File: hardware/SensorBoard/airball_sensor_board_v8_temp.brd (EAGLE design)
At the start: 19.1 x 6.3 mm, 3 parts, among them J2 Vertical Qwiic Connector, U1 TMP102

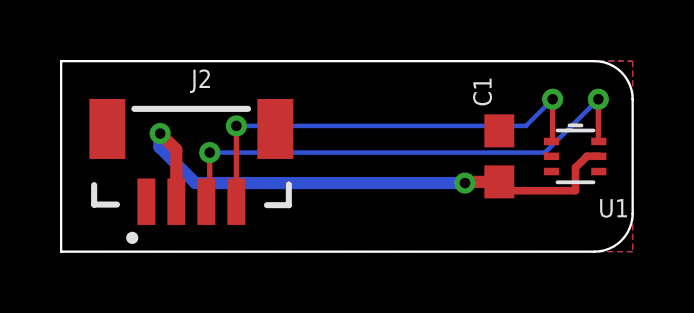
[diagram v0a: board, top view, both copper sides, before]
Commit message: Completed temperature sensor board.
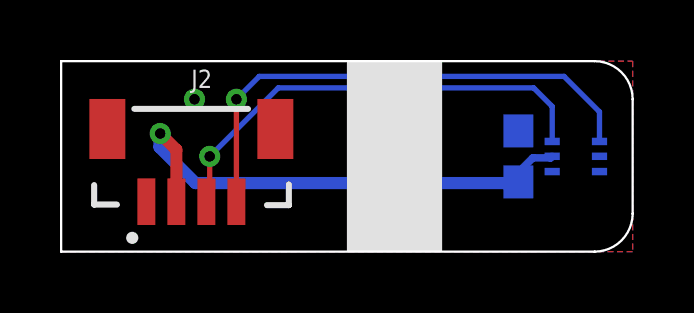
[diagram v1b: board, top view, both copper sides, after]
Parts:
- moved C1 0.63 mm to (15.2, 3.17), flipped to the bottom
- flipped U1 to the bottom
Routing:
- net SCL: track 14.9 -> 17.3 mm, vias 2 -> 1
- net VCC: track 19.2 -> 17.5 mm, vias 2 -> 1
- net SDA: track 16.9 -> 15.3 mm, vias 2 -> 1
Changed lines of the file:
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@@
 <setting verticaltext="up"/>
 </settings>
-<grid distance="25" unitdist="mil" unit="mil" style="lines" multiple="1" display="yes" altdistance="5" altunitdist="mil" altunit="mil"/>
+<grid distance="5" unitdist="mil" unit="mil" style="lines" multiple="1" display="yes" altdistance="5" altunitdist="mil" altunit="mil"/>
 <layers>
 <layer number="1" name="Top" color="4" fill="1" visible="yes" active="yes"/>
@@
 <wire x1="17.78" y1="6.35" x2="0" y2="6.35" width="0.0762" layer="20"/>
 <wire x1="0" y1="0" x2="0" y2="6.35" width="0.0762" layer="20"/>
+<rectangle x1="9.525" y1="0" x2="12.7" y2="6.35" layer="21"/>
 </plain>
 <attributes>
@@
 </autorouter>
 <elements>
-<element name="C1" library="SparkFun-Capacitors" package="0603" value="4.7uF" x="14.605" y="3.175" smashed="yes" rot="R90">
-<attribute name="NAME" x="14.351" y="5.334" size="0.6096" layer="25" font="vector" ratio="20" rot="R90" align="bottom-center"/>
-<attribute name="PROD_ID" value="CAP-08280" x="24.765" y="22.225" size="1.778" layer="27" rot="R90" display="off"/>
-<attribute name="VALUE" x="12.954" y="4.572" size="0.6096" layer="27" font="vector" ratio="20" rot="R90" align="top-center"/>
+<element name="C1" library="SparkFun-Capacitors" package="0603" value="4.7uF" x="15.24" y="3.175" smashed="yes" rot="MR90">
+<attribute name="NAME" x="15.494" y="5.334" size="0.6096" layer="26" font="vector" ratio="20" rot="MR90" align="bottom-center"/>
+<attribute name="PROD_ID" value="CAP-08280" x="5.08" y="22.225" size="1.778" layer="28" rot="MR90" display="off"/>
+<attribute name="VALUE" x="16.891" y="4.572" size="0.6096" layer="28" font="vector" ratio="20" rot="MR90" align="top-center"/>
 </element>
 <element name="J2" library="SparkFun-Connectors" package="JST04_1MM_VERT" value="Vertical Qwiic Connector" x="4.318" y="0.889" smashed="yes">
@@
 <attribute name="PROD_ID" value="CONN-14483" x="27.178" y="-1.651" size="1.778" layer="27" display="off"/>
 </element>
-<element name="U1" library="SparkFun-Sensors" package="SOT563" value="TMP102" x="17.145" y="3.175" smashed="yes">
-<attribute name="NAME" x="18.415" y="1.143" size="0.6096" layer="25" font="vector" ratio="20" align="bottom-center"/>
-<attribute name="PROD_ID" value="IC-09303" x="32.385" y="-6.985" size="1.778" layer="27" display="off"/>
-<attribute name="VALUE" x="17.145" y="1.016" size="0.6096" layer="27" font="vector" ratio="20" align="top-center"/>
+<element name="U1" library="SparkFun-Sensors" package="SOT563" value="TMP102" x="17.145" y="3.175" smashed="yes" rot="MR0">
+<attribute name="NAME" x="15.875" y="1.143" size="0.6096" layer="26" font="vector" ratio="20" rot="MR0" align="bottom-center"/>
+<attribute name="PROD_ID" value="IC-09303" x="1.905" y="-6.985" size="1.778" layer="28" rot="MR0" display="off"/>
+<attribute name="VALUE" x="17.145" y="1.016" size="0.6096" layer="28" font="vector" ratio="20" rot="MR0" align="top-center"/>
 </element>
 </elements>
@@
 <contactref element="C1" pad="1"/>
 <contactref element="J2" pad="2"/>
-<wire x1="17.921415625" y1="3.178303125" x2="17.526" y2="3.178303125" width="0.254" layer="1"/>
-<wire x1="17.526" y1="3.178303125" x2="17.145" y2="2.797303125" width="0.254" layer="1"/>
-<wire x1="17.145" y1="2.797303125" x2="17.145" y2="2.032" width="0.254" layer="1"/>
-<wire x1="17.145" y1="2.032" x2="14.898" y2="2.032" width="0.254" layer="1"/>
-<wire x1="14.898" y1="2.032" x2="14.605" y2="2.325" width="0.2032" layer="1"/>
+<wire x1="15.533" y1="2.032" x2="15.24" y2="2.325" width="0.2032" layer="16"/>
 <via x="3.302" y="3.937" extent="1-16" drill="0.35"/>
 <wire x1="3.84" y1="1.664" x2="3.84" y2="3.399" width="0.4064" layer="1"/>
 <wire x1="3.84" y1="3.399" x2="3.302" y2="3.937" width="0.4064" layer="1"/>
-<wire x1="3.2776" y1="3.48425625" x2="4.47585625" y2="2.286" width="0.4064" layer="16"/>
-<wire x1="4.47585625" y1="2.286" x2="13.462" y2="2.286" width="0.4064" layer="16"/>
 <wire x1="3.302" y1="3.937" x2="3.2776" y2="3.9126" width="0.4064" layer="16"/>
 <wire x1="3.2776" y1="3.9126" x2="3.2776" y2="3.48425625" width="0.4064" layer="16"/>
-<via x="13.462" y="2.286" extent="1-16" drill="0.35"/>
-<wire x1="13.462" y1="2.286" x2="13.501" y2="2.325" width="0.4064" layer="1"/>
-<wire x1="13.501" y1="2.325" x2="14.605" y2="2.325" width="0.4064" layer="1"/>
+<wire x1="15.201" y1="2.286" x2="15.24" y2="2.325" width="0.4064" layer="16"/>
+<wire x1="4.47585625" y1="2.286" x2="15.201" y2="2.286" width="0.4064" layer="16"/>
+<wire x1="3.2776" y1="3.48425625" x2="4.47585625" y2="2.286" width="0.4064" layer="16"/>
+<wire x1="16.368584375" y1="3.178303125" x2="16.3159" y2="3.12561875" width="0.254" layer="16"/>
+<wire x1="16.3159" y1="3.12561875" x2="15.72306875" y2="3.12561875" width="0.254" layer="16"/>
+<wire x1="15.24" y1="2.64255" x2="15.24" y2="2.325" width="0.254" layer="16"/>
+<wire x1="15.72306875" y1="3.12561875" x2="15.24" y2="2.64255" width="0.254" layer="16"/>
 </signal>
 <signal name="GND">
@@
 <vertex x="0" y="0"/>
 </polygon>
+<via x="10.16" y="1.27" extent="1-16" drill="0.35"/>
+<via x="10.16" y="3.81" extent="1-16" drill="0.35"/>
+<via x="4.445" y="5.08" extent="1-16" drill="0.35"/>
 </signal>
 <signal name="SDA">
 <contactref element="U1" pad="6"/>
 <contactref element="J2" pad="3"/>
-<via x="17.907" y="5.08" extent="1-16" drill="0.35"/>
-<wire x1="17.907" y1="5.08" x2="16.129" y2="3.302" width="0.1524" layer="16"/>
-<wire x1="16.129" y1="3.302" x2="4.953" y2="3.302" width="0.1524" layer="16"/>
-<wire x1="4.953" y1="3.302" x2="4.826" y2="3.302" width="0.1524" layer="16"/>
-<via x="4.953" y="3.302" extent="1-16" drill="0.35"/>
-<wire x1="4.953" y1="3.302" x2="4.953" y2="1.777" width="0.1778" layer="1"/>
+<via x="4.953" y="3.175" extent="1-16" drill="0.35"/>
+<wire x1="4.953" y1="3.175" x2="4.953" y2="1.777" width="0.1778" layer="1"/>
 <wire x1="4.953" y1="1.777" x2="4.84" y2="1.664" width="0.1778" layer="1"/>
-<wire x1="17.907" y1="5.08" x2="17.907" y2="3.687384375" width="0.1778" layer="1"/>
-<wire x1="17.907" y1="3.687384375" x2="17.921415625" y2="3.67296875" width="0.1778" layer="1"/>
+<wire x1="4.953" y1="3.175" x2="7.2372" y2="5.4592" width="0.1778" layer="16"/>
+<wire x1="16.368584375" y1="4.840415625" x2="16.368584375" y2="3.67296875" width="0.1778" layer="16"/>
+<wire x1="7.2372" y1="5.4592" x2="15.7498" y2="5.4592" width="0.1778" layer="16"/>
+<wire x1="15.7498" y1="5.4592" x2="16.368584375" y2="4.840415625" width="0.1778" layer="16"/>
 </signal>
 <signal name="SCL">
 <contactref element="J2" pad="4"/>
 <contactref element="U1" pad="1"/>
-<via x="16.383" y="5.08" extent="1-16" drill="0.35"/>
-<wire x1="16.383" y1="5.08" x2="15.494" y2="4.191" width="0.1524" layer="16"/>
-<wire x1="15.494" y1="4.191" x2="5.842" y2="4.191" width="0.1524" layer="16"/>
-<via x="5.842" y="4.191" extent="1-16" drill="0.35"/>
-<wire x1="5.842" y1="4.191" x2="5.842" y2="1.666" width="0.1778" layer="1"/>
-<wire x1="5.842" y1="1.666" x2="5.84" y2="1.664" width="0.1778" layer="1"/>
-<wire x1="16.383" y1="5.08" x2="16.383" y2="3.71096875" width="0.1778" layer="1"/>
-<wire x1="16.383" y1="3.71096875" x2="16.345" y2="3.67296875" width="0.1778" layer="1"/>
+<via x="5.842" y="5.08" extent="1-16" drill="0.35"/>
+<wire x1="5.84" y1="1.664" x2="5.842" y2="1.666" width="0.1778" layer="1"/>
+<wire x1="5.842" y1="5.08" x2="5.842" y2="1.666" width="0.1778" layer="1"/>
+<wire x1="5.842" y1="5.08" x2="6.604" y2="5.842" width="0.1778" layer="16"/>
+<wire x1="6.604" y1="5.842" x2="16.764" y2="5.842" width="0.1778" layer="16"/>
+<wire x1="16.764" y1="5.842" x2="17.945" y2="4.661" width="0.1778" layer="16"/>
+<wire x1="17.945" y1="4.661" x2="17.945" y2="3.67296875" width="0.1778" layer="16"/>
 </signal>
 </signals>
